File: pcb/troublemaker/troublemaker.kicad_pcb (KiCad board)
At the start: 2 copper layers, 419 x 394 mm, 111 parts, among them IC1 TEENSY_4.1, J1 neopixel_data_RPI19_GPIO10, J2 taptempo_led_RPI16_GPIO23, J3 5V_RPI2_OR_4, J4 GND_RPI34, J5 Conn_01x12, SW1 sw_eq2, SW10 sw_grain_playback, SW11 btn_sampler_stop, SW2 sw_eq1, SW3 sw_sub, SW4 sw_bass, SW5 sw_mid, SW6 sw_high, SW7 btn_delay_taptempo, SW8 sw_delay_type, SW9 sw_grain_type, U2 CD74HC4067M, U3 CD74HC4067M, U4 CD74HC4067M, U5 CD74HC4067M, U6 CD74HC4067M

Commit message: added expansion port and GPIO socket
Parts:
- removed J2: taptempo_led_RPI16_GPIO23, Connector_PinHeader_1.00mm:PinHeader_1x01_P1.00mm_Vertical
- removed the J3 at (174.2, 265.2)
- removed the J4 at (174.2, 225.2)
- added J25: EXPANSION_PORT, Connector_IDC:IDC-Header_2x17_P2.54mm_Vertical, B.Cu at (264.6, 243.0)
- added J3: 5V_RPI2_OR_4, Connector_PinHeader_1.00mm:PinHeader_1x01_P1.00mm_Vertical, B.Cu at (178.5, 271.0)
- added J3: 5V_RPI2_OR_4, Connector_PinHeader_1.00mm:PinHeader_1x01_P1.00mm_Vertical, B.Cu at (174.5, 271.0)
- added J4: GND_RPI34, Connector_PinHeader_1.00mm:PinHeader_1x01_P1.00mm_Vertical, B.Cu at (174.5, 263.8)
- added J4: GND_RPI34, Connector_PinHeader_1.00mm:PinHeader_1x01_P1.00mm_Vertical, B.Cu at (178.5, 263.8)
- added SW12: sw_input_mode, Library:SW_SPDT_red_leozor, B.Cu at (204.0, 205.2)
- J1: value neopixel_data_RPI19_GPIO10 -> RPi_GPIO; footprint Connector_PinHeader_1.00mm:PinHeader_1x01_P1.00mm_Vertical -> Connector_IDC:IDC-Header_2x20_P2.54mm_Vertical
- Neopixel_bass_gain_reduction1, Neopixel_bass_out_level1, Neopixel_high_gain_reduction1, Neopixel_high_out_level1, Neopixel_mid_gain_reduction1, Neopixel_mid_out_level1, Neopixel_sub_gain_reduction1, Neopixel_sub_out_level1: footprint leozorLib:Neopixel-8LED -> Library:Neopixel-8LED
- SW1, SW10, SW2, SW3, SW4, SW5, SW6, SW8, SW9: footprint leozorLib:SW_SPDT_red_leozor -> Library:SW_SPDT_red_leozor
- SW11, SW7: footprint leozorLib:arcade_service_button_leozor -> Library:arcade_service_button_leozor
- U2, U3, U4, U5, U6: footprint leozorLib:Breakout_HC4067_PTH_Only -> Library:Breakout_HC4067_PTH_Only
- moved J1 35.2 mm to (196.0, 272.7), turned to 0 degrees
- moved U6 8.31 mm to (316.5, 359.5)
- moved RASPBERRY PI 4 5.59 mm to (141.0, 238.5)
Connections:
- IC1 pad 33: unconnected-(IC1-MCLK2-Pad33) -> XT_Teensy33
- IC1 pad 34: unconnected-(IC1-RX8-Pad34) -> XT_Teensy34
- IC1 pad 35: unconnected-(IC1-TX8-Pad35) -> XT_Teensy35
- IC1 pad 36: unconnected-(IC1-CS_2-Pad36) -> XT_Teensy36
- IC1 pad 37: unconnected-(IC1-CS_3-Pad37) -> XT_Teensy37
- IC1 pad 40: unconnected-(IC1-A16-Pad40) -> XT_Teensy40
- IC1 pad 41: unconnected-(IC1-A17-Pad41) -> XT_Teensy41
- IC1 pad 69: GND -> XT_GND
- IC1 pad 70: GND -> XT_GND
- IC1 pad 71: GND -> XT_GND
- J1 pad 1: neopixel_data -> unconnected-(J1-Pin_1-Pad1)
- J5 pad 12: GND -> XT_GND
- Neopixel_sub_gain_reduction1 pad 5: GND -> XT_GND
- Neopixel_sub_gain_reduction1 pad 7: +5V -> XT_RPi_5v
- Neopixel_sub_gain_reduction1 pad 8: GND -> XT_GND
- R1 pad 1: taptempo_LED -> taptempo_LED_RPi16
- RV1 pad 3: GND -> XT_GND
- RV10 pad 3: GND -> XT_GND
- RV11 pad 3: GND -> XT_GND
- RV12 pad 3: GND -> XT_GND
- RV13 pad 3: GND -> XT_GND
- RV14 pad 3: GND -> XT_GND
- RV15 pad 3: GND -> XT_GND
- RV16 pad 3: GND -> XT_GND
- RV17 pad 3: GND -> XT_GND
- RV18 pad 3: GND -> XT_GND
- RV19 pad 3: GND -> XT_GND
- RV2 pad 3: GND -> XT_GND
- RV20 pad 3: GND -> XT_GND
- RV21 pad 3: GND -> XT_GND
- RV22 pad 3: GND -> XT_GND
- RV23 pad 3: GND -> XT_GND
- RV24 pad 3: GND -> XT_GND
- RV25 pad 3: GND -> XT_GND
- RV26 pad 3: GND -> XT_GND
- RV27 pad 3: GND -> XT_GND
- RV28 pad 3: GND -> XT_GND
- RV29 pad 3: GND -> XT_GND
- RV3 pad 3: GND -> XT_GND
- RV30 pad 3: GND -> XT_GND
- RV31 pad 3: GND -> XT_GND
- RV32 pad 3: GND -> XT_GND
- RV33 pad 3: GND -> XT_GND
- RV34 pad 3: GND -> XT_GND
- RV35 pad 3: GND -> XT_GND
- RV36 pad 3: GND -> XT_GND
- RV37 pad 3: GND -> XT_GND
- RV38 pad 3: GND -> XT_GND
- RV39 pad 3: GND -> XT_GND
- RV4 pad 3: GND -> XT_GND
- RV47 pad 3: GND -> XT_GND
- RV48 pad 3: GND -> XT_GND
- RV49 pad 3: GND -> XT_GND
- RV5 pad 3: GND -> XT_GND
- RV50 pad 3: GND -> XT_GND
- RV51 pad 3: GND -> XT_GND
- RV52 pad 3: GND -> XT_GND
- RV53 pad 3: GND -> XT_GND
- RV54 pad 3: GND -> XT_GND
- RV55 pad 3: GND -> XT_GND
- RV56 pad 3: GND -> XT_GND
- RV57 pad 3: GND -> XT_GND
- RV58 pad 3: GND -> XT_GND
- RV59 pad 3: GND -> XT_GND
- RV6 pad 3: GND -> XT_GND
- RV60 pad 3: GND -> XT_GND
- RV61 pad 3: GND -> XT_GND
- RV62 pad 3: GND -> XT_GND
- RV63 pad 3: GND -> XT_GND
- RV64 pad 3: GND -> XT_GND
- RV65 pad 3: GND -> XT_GND
- RV66 pad 3: GND -> XT_GND
- RV67 pad 3: GND -> XT_GND
- RV68 pad 3: GND -> XT_GND
- RV69 pad 3: GND -> XT_GND
- RV7 pad 3: GND -> XT_GND
- RV70 pad 3: GND -> XT_GND
- RV71 pad 3: GND -> XT_GND
- RV72 pad 3: GND -> XT_GND
- RV73 pad 3: GND -> XT_GND
- RV74 pad 3: GND -> XT_GND
- RV75 pad 3: GND -> XT_GND
- RV76 pad 3: GND -> XT_GND
- RV77 pad 3: GND -> XT_GND
- RV78 pad 3: GND -> XT_GND
- RV79 pad 3: GND -> XT_GND
- RV8 pad 3: GND -> XT_GND
- RV80 pad 3: GND -> XT_GND
- RV81 pad 3: GND -> XT_GND
- RV82 pad 3: GND -> XT_GND
- RV83 pad 3: GND -> XT_GND
- RV84 pad 3: GND -> XT_GND
- RV85 pad 3: GND -> XT_GND
- RV9 pad 3: GND -> XT_GND
- SW1 pad 2: GND -> XT_GND
- SW10 pad 2: GND -> XT_GND
- SW11 pad 1: GND -> XT_GND
- SW2 pad 2: GND -> XT_GND
- SW3 pad 2: GND -> XT_GND
- SW4 pad 2: GND -> XT_GND
- SW5 pad 2: GND -> XT_GND
- SW6 pad 2: GND -> XT_GND
- SW7 pad 1: GND -> XT_GND
- SW8 pad 2: GND -> XT_GND
- SW9 pad 2: GND -> XT_GND
- U2 pad 12: GND -> XT_GND
- U3 pad 12: GND -> XT_GND
- U4 pad 12: GND -> XT_GND
- U5 pad 12: GND -> XT_GND
- U6 pad 12: GND -> XT_GND
- taptempo_led1 pad 1: GND -> XT_GND
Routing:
- net XT_GND: track 0.00 -> 4341.1 mm, vias 0 -> 8
- net GND: track 4254.6 -> 0.00 mm, vias 8 -> 0
- net XT_RPi_5v: track 0.00 -> 291.5 mm, vias 0 -> 3
- net +5V: track 174.7 -> 0.00 mm, vias 3 -> 0
- net sw_input_mode_RPi21: track 0.00 -> 102.1 mm, vias 0 -> 2
- net XT_RPi33: track 0.00 -> 70.2 mm
- net XT_RPi32: track 0.00 -> 67.6 mm
- net XT_RPi10: track 0.00 -> 65.4 mm
- net XT_RPi7: track 0.00 -> 62.3 mm
- net XT_RPi11: track 0.00 -> 59.7 mm
- net XT_RPi8: track 0.00 -> 59.6 mm, vias 0 -> 2
- net XT_RPi36: track 0.00 -> 59.0 mm
- net XT_RPi13: track 0.00 -> 58.4 mm
- net XT_RPi31: track 0.00 -> 58.3 mm
- net XT_Teensy33: track 0.00 -> 57.8 mm
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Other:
- board text added: "Expansion port"
- board text added: "FAN_5V"
- board text added: "FAN_GND"
- board text added: "Raspberry Pi GPIO"
- board text added: "TROUBLEMAKER V1"
- board text removed: "+5V PIN 2 OR 4"
- board text removed: "NEOPIXEL DATA PIN19 GPIO10"
- board text removed: "TAPTEMPO LED PIN16 GPIO23"

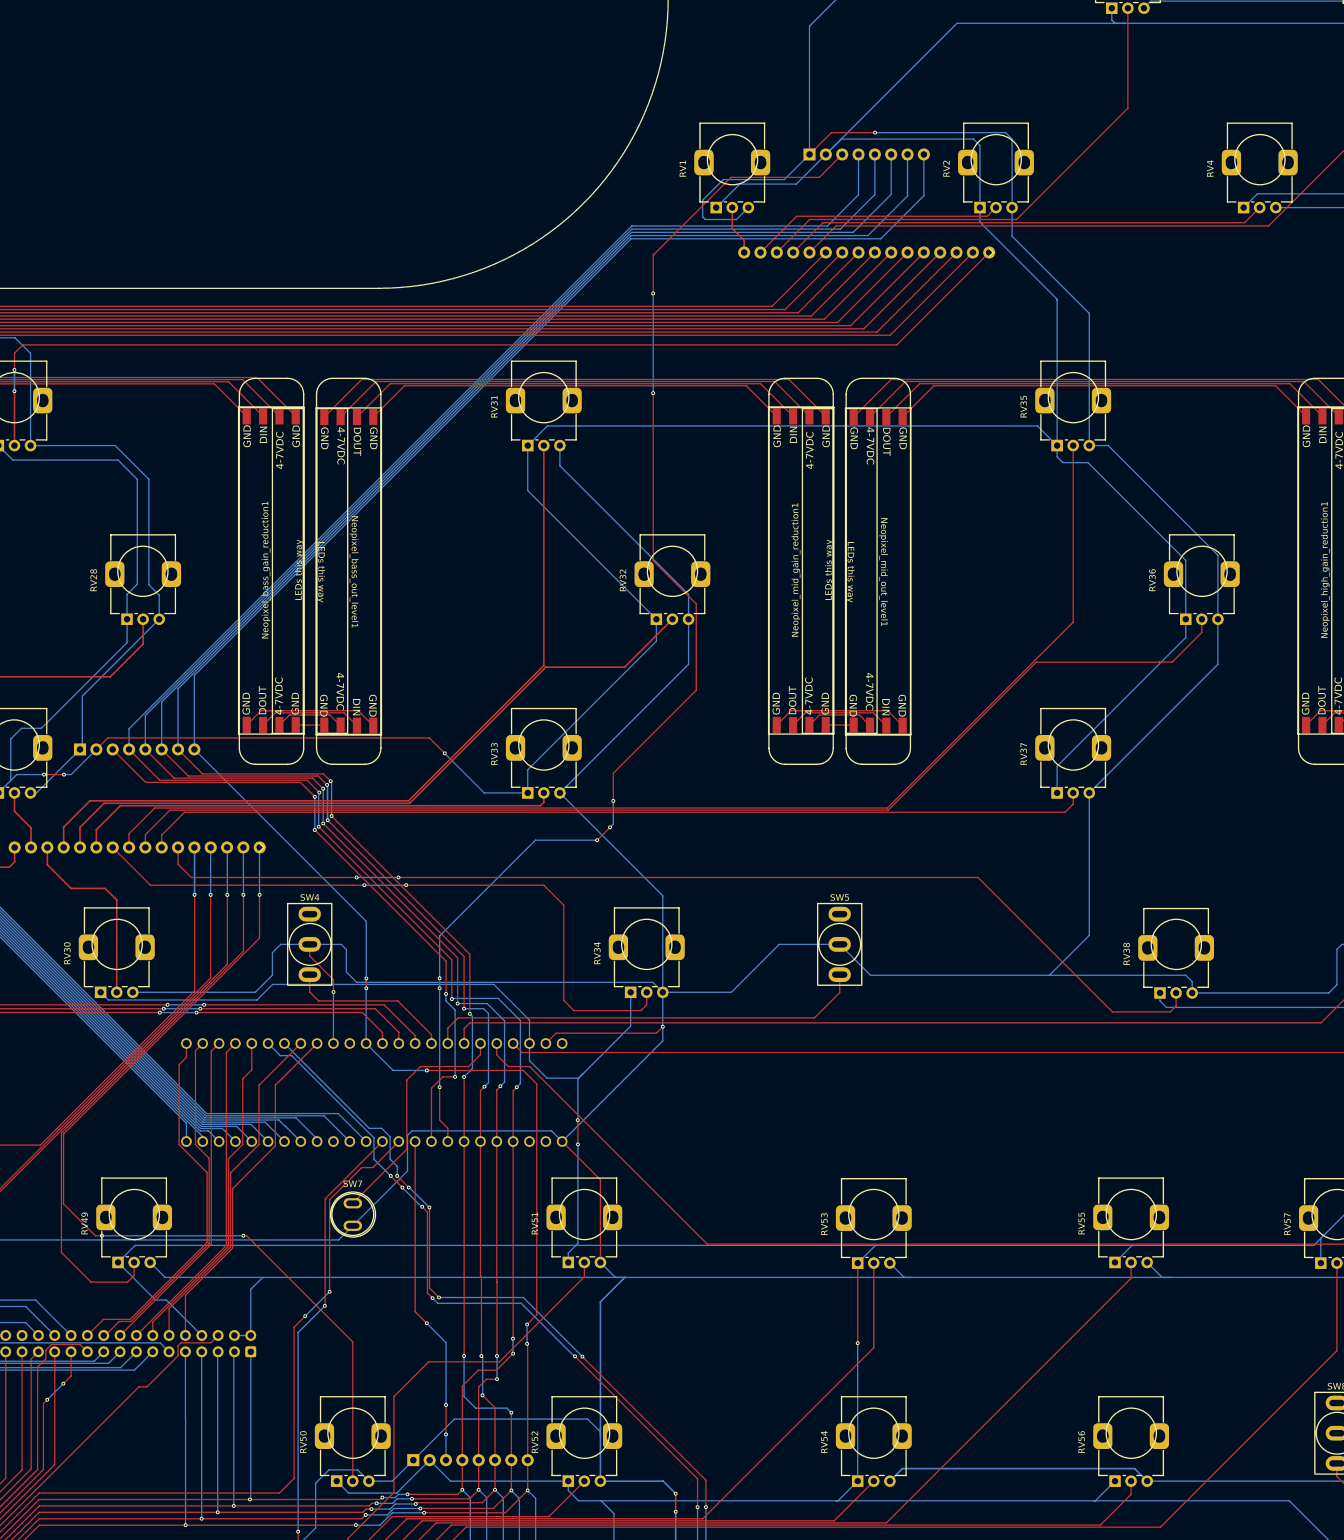
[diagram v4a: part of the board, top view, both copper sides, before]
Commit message: added mooncrown logo
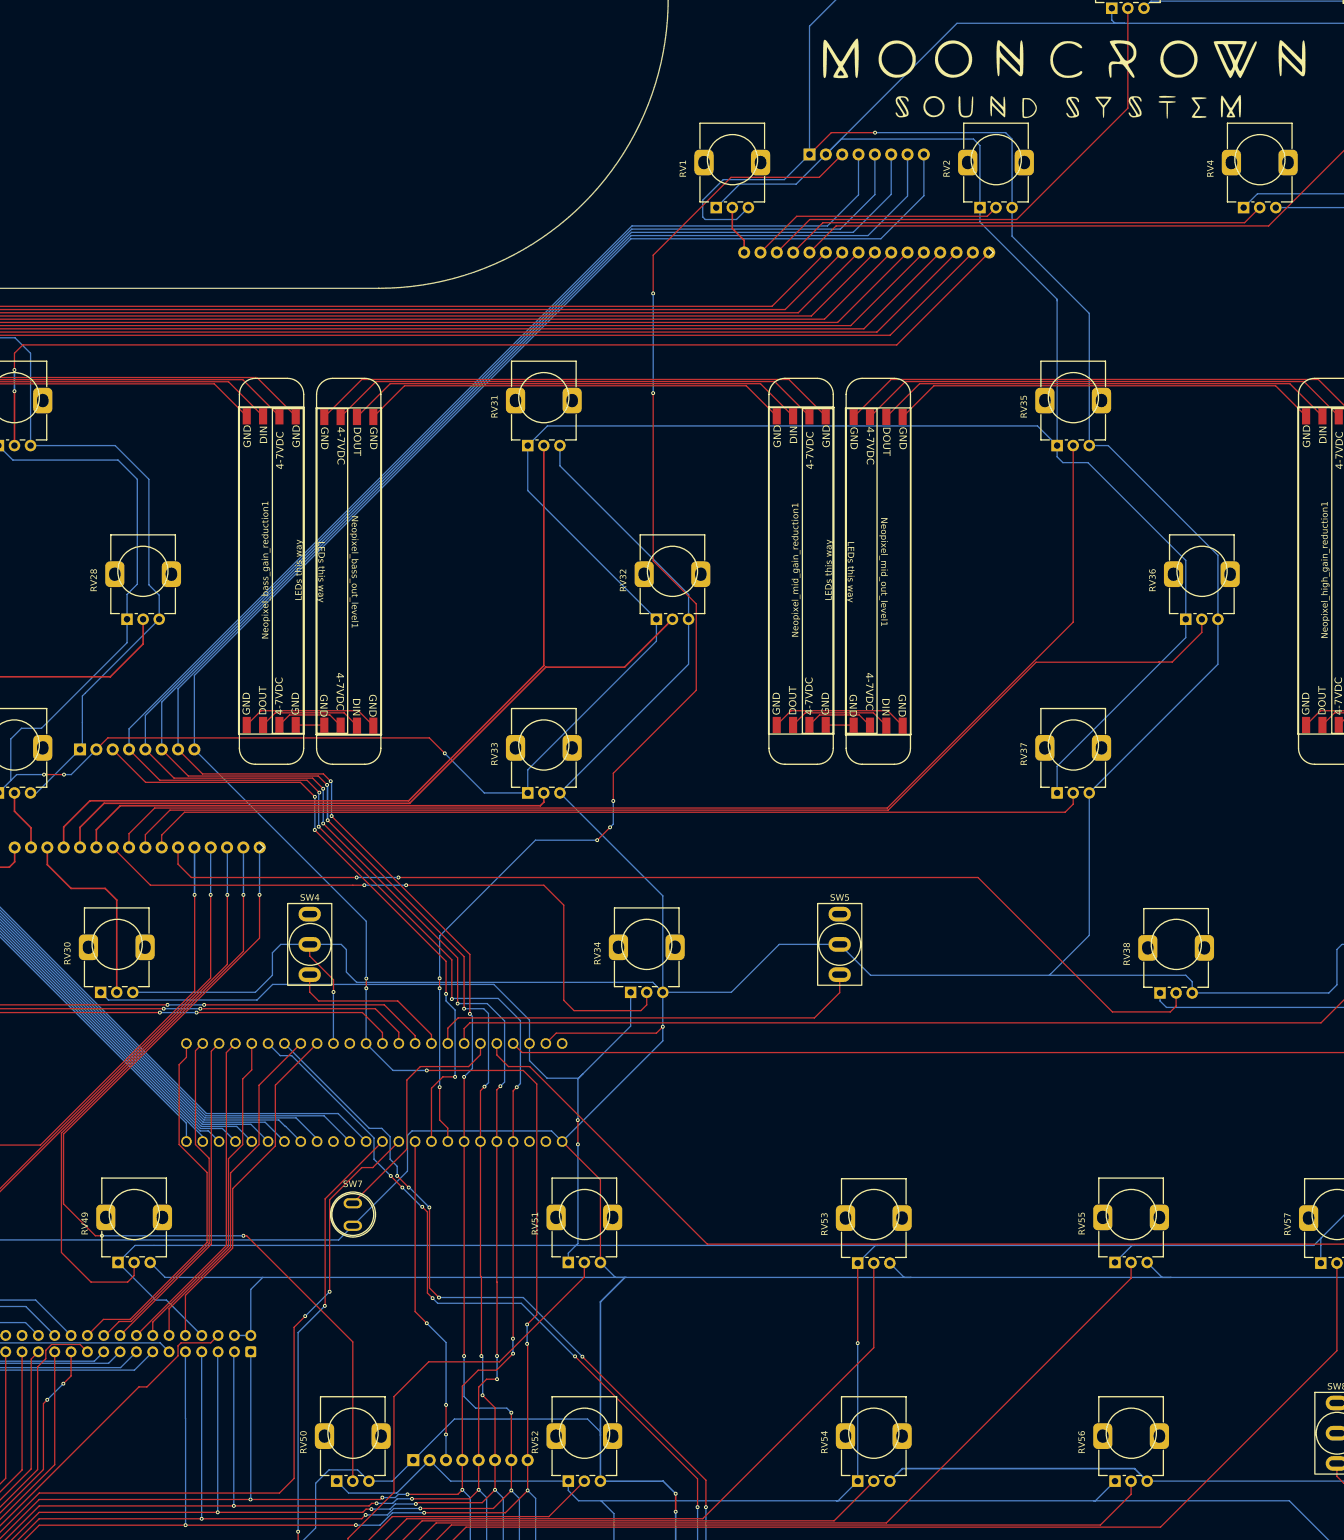
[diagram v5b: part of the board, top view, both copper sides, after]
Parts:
- added Ref**: Val**, Silkscreen:TestSilkscreen, F.Cu at (391.1, 45.1)

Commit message: Cleaned PCB traces
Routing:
- net XT_GND: track 4341.1 -> 4309.1 mm
- net 3v3: track 3747.7 -> 3744.3 mm
